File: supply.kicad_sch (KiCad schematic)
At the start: 42 parts

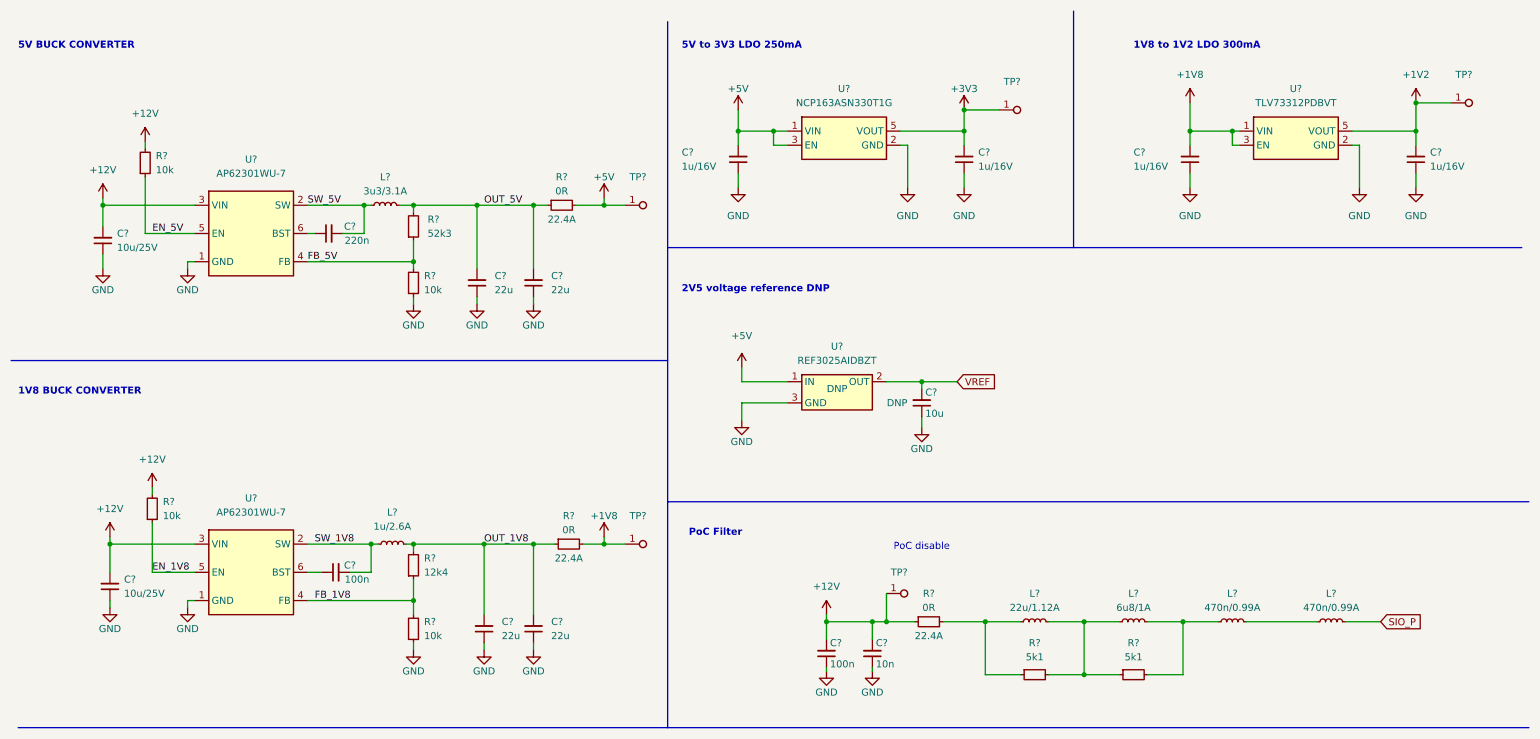
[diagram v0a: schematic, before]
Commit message: Anotate components and fix ERC errors and warnings
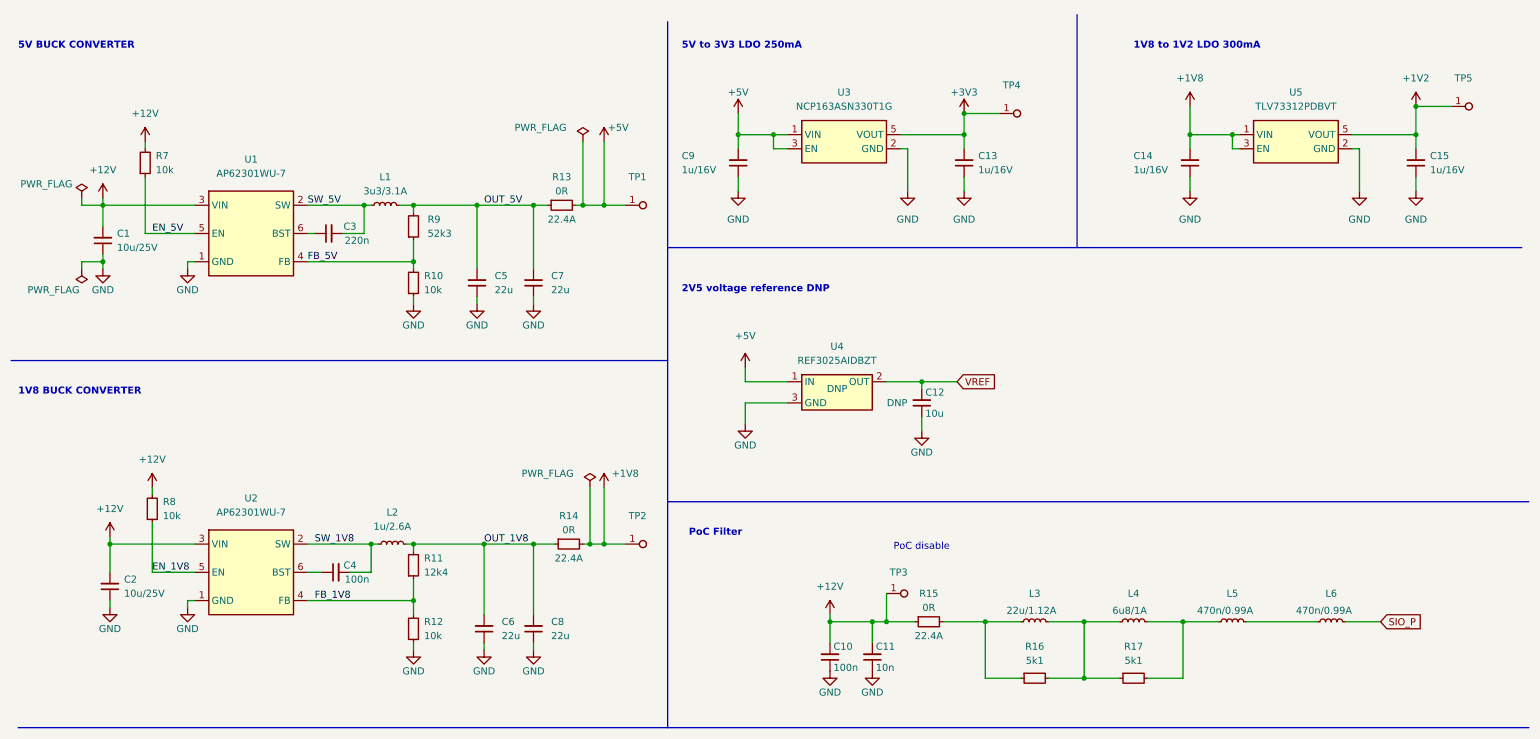
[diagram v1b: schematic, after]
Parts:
- L3: renamed from L?; ISat 0.97A -> 1.12A
- L4: renamed from L?; ISat 1.4 A -> 1 A
- L5, L6: renamed from L?; ISat 0.76 A -> 0.99 A
- gave numbers to parts that had none: 38
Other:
- moved on the sheet: C10, C11, C13, C14, C15, C9, R16, R17, TP4, TP5, U3, U5

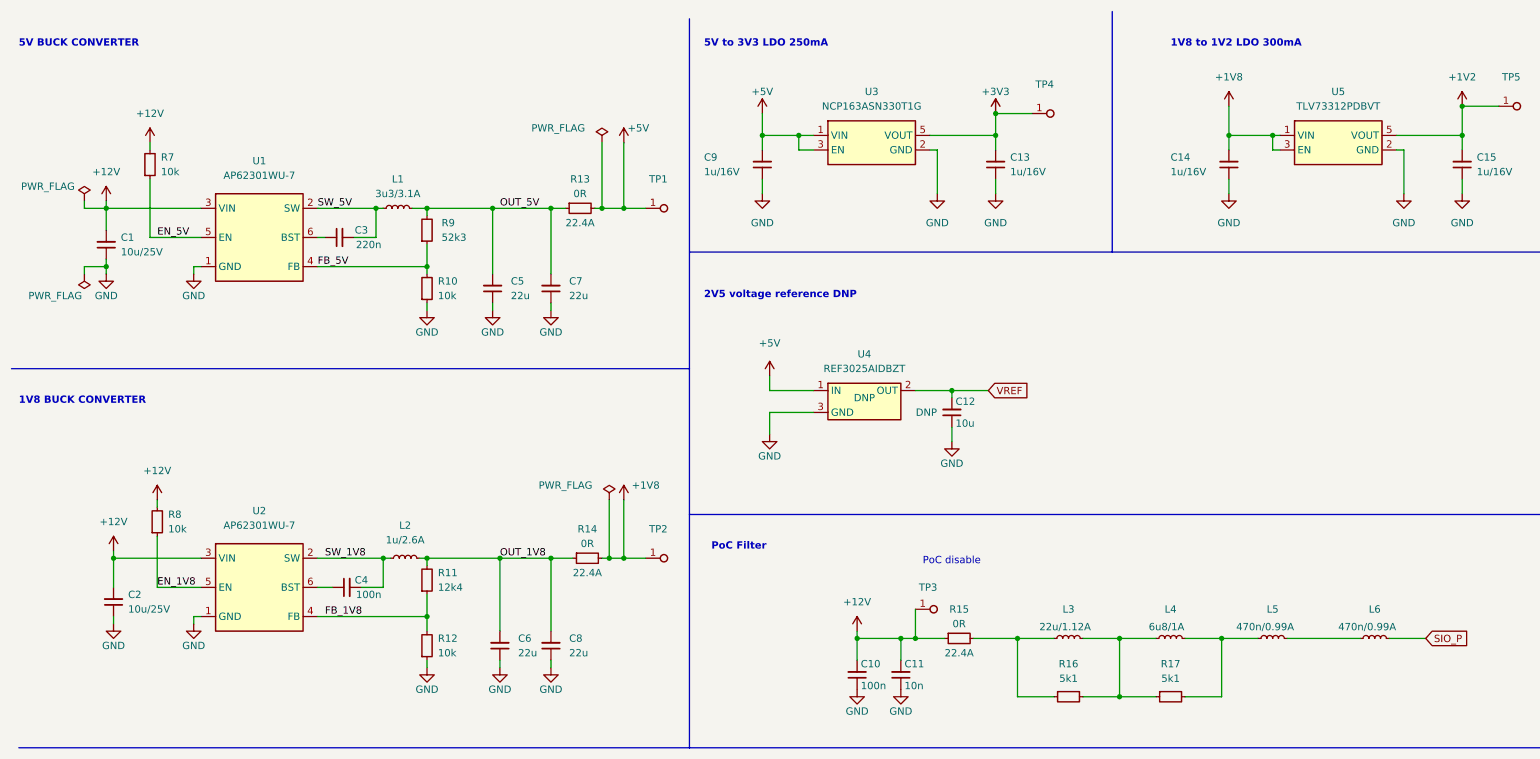
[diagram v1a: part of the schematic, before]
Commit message: Implement changes suggested in design review to schematics
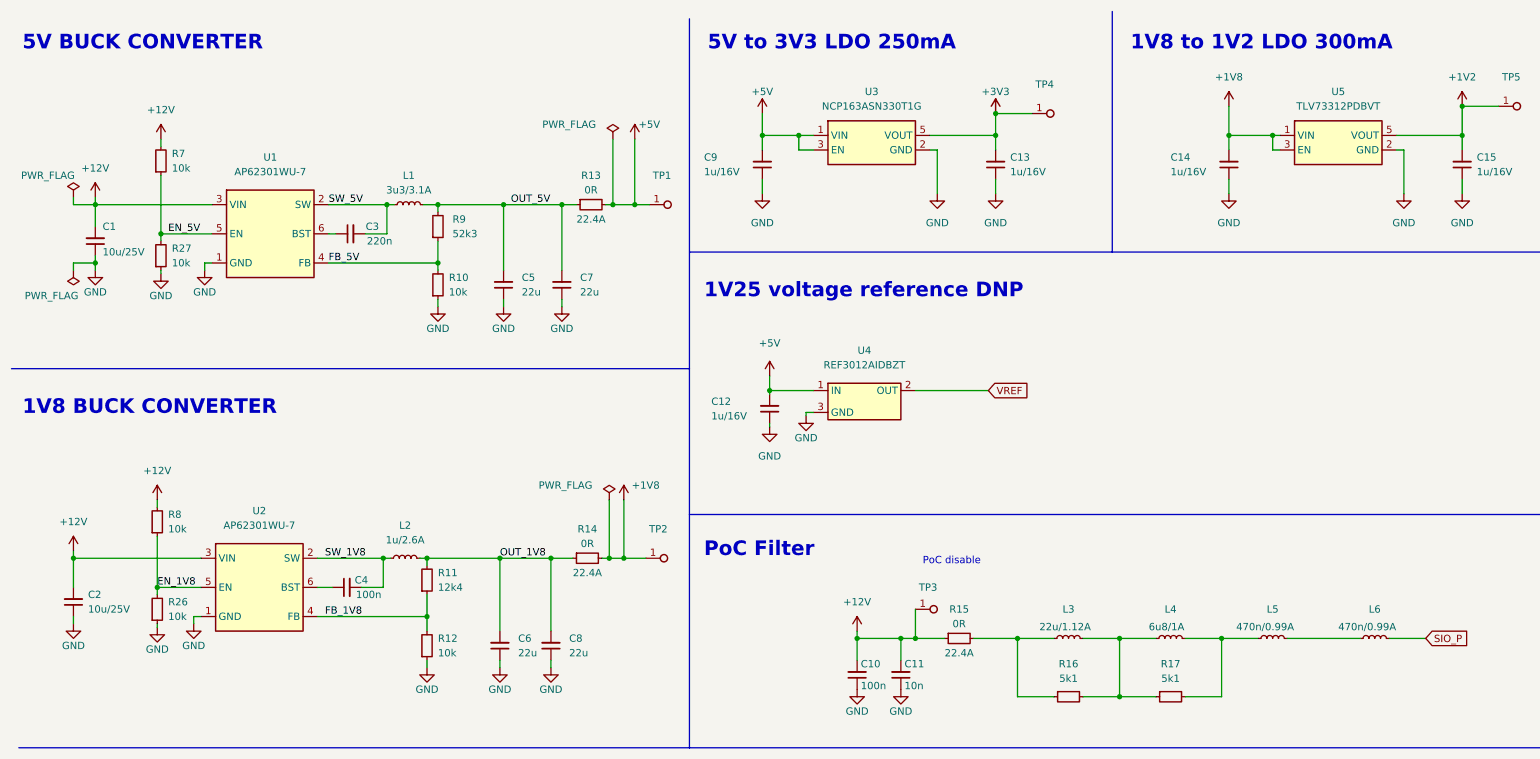
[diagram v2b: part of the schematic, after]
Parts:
- removed C12: C_10u_0402, antmicro-footprints:C_0402_1005Metric, symbol antmicroCapacitors0402:C_10u_0402
- removed U4: REF3025AIDBZT, antmicro-footprints:SOT-23-3, symbol antmicroPMICPowerDistributionSwitchesLoadDrivers:REF3025AIDBZT
- added C12: C_1u_16V_0402, antmicro-footprints:C_0402_1005Metric, symbol antmicroCapacitors0402:C_1u_16V_0402
- added R26, R27: R_10k_0402, antmicro-footprints:R_0402_1005Metric, symbol antmicroResistors0402:R_10k_0402
- added U4: REF3012AIDBZT, antmicro-footprints:SOT-23-3, symbol antmicroPMICPowerDistributionSwitchesLoadDrivers:REF3012AIDBZT
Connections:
- net +5V: now also C12.2, U4.1 (IN)
- net EN_1V8: now also R26.2
- net EN_5V: now also R27.2
- net GND: now also C12.1, R26.1, R27.1, U4.3 (GND)
- net VREF: now also U4.2 (OUT)
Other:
- note added: "1V25 voltage reference DNP"
- note removed: "2V5 voltage reference DNP"
- moved on the sheet: C1, C2, C3, C5, C7, L1, R10, R13, R7, R9, TP1, U1

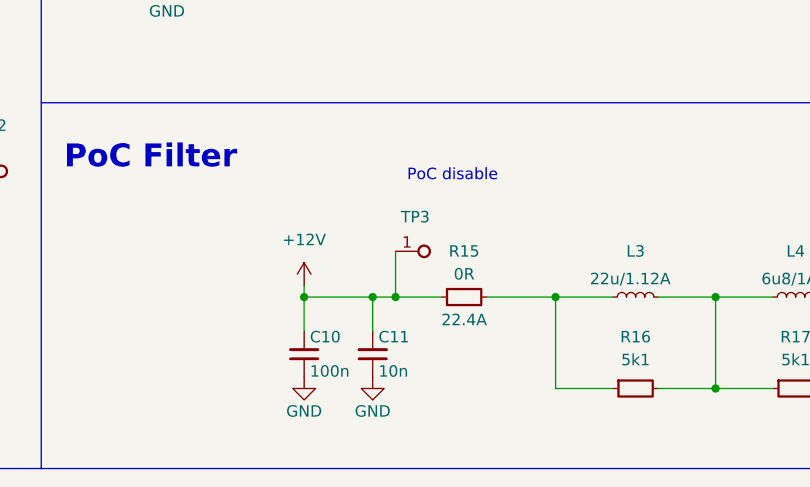
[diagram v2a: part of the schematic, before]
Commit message: Remove R15 and anotate schematic
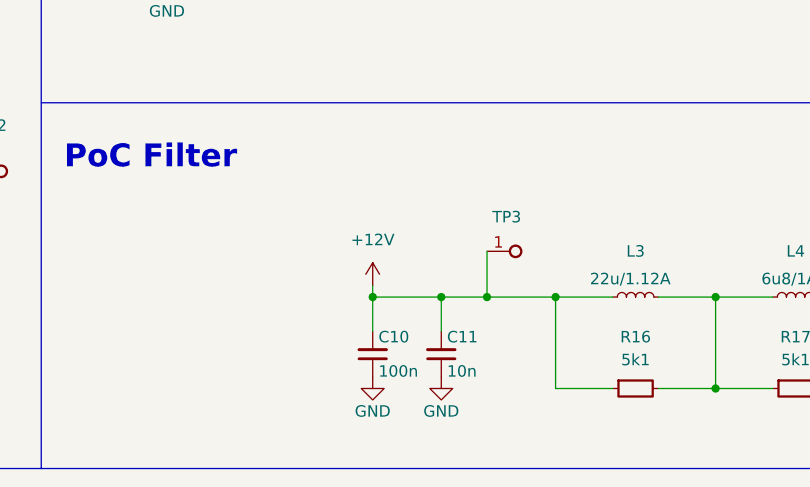
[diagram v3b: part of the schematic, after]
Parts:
- removed R15: R_0R_22.4A_0603, antmicro-footprints:R_0603_1608Metric, symbol antmicroResistors0603:R_0R_22.4A_0603
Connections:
- net +12V: now also L3.1, R16.1
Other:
- note removed: "PoC disable"
- moved on the sheet: C10, C11, TP3

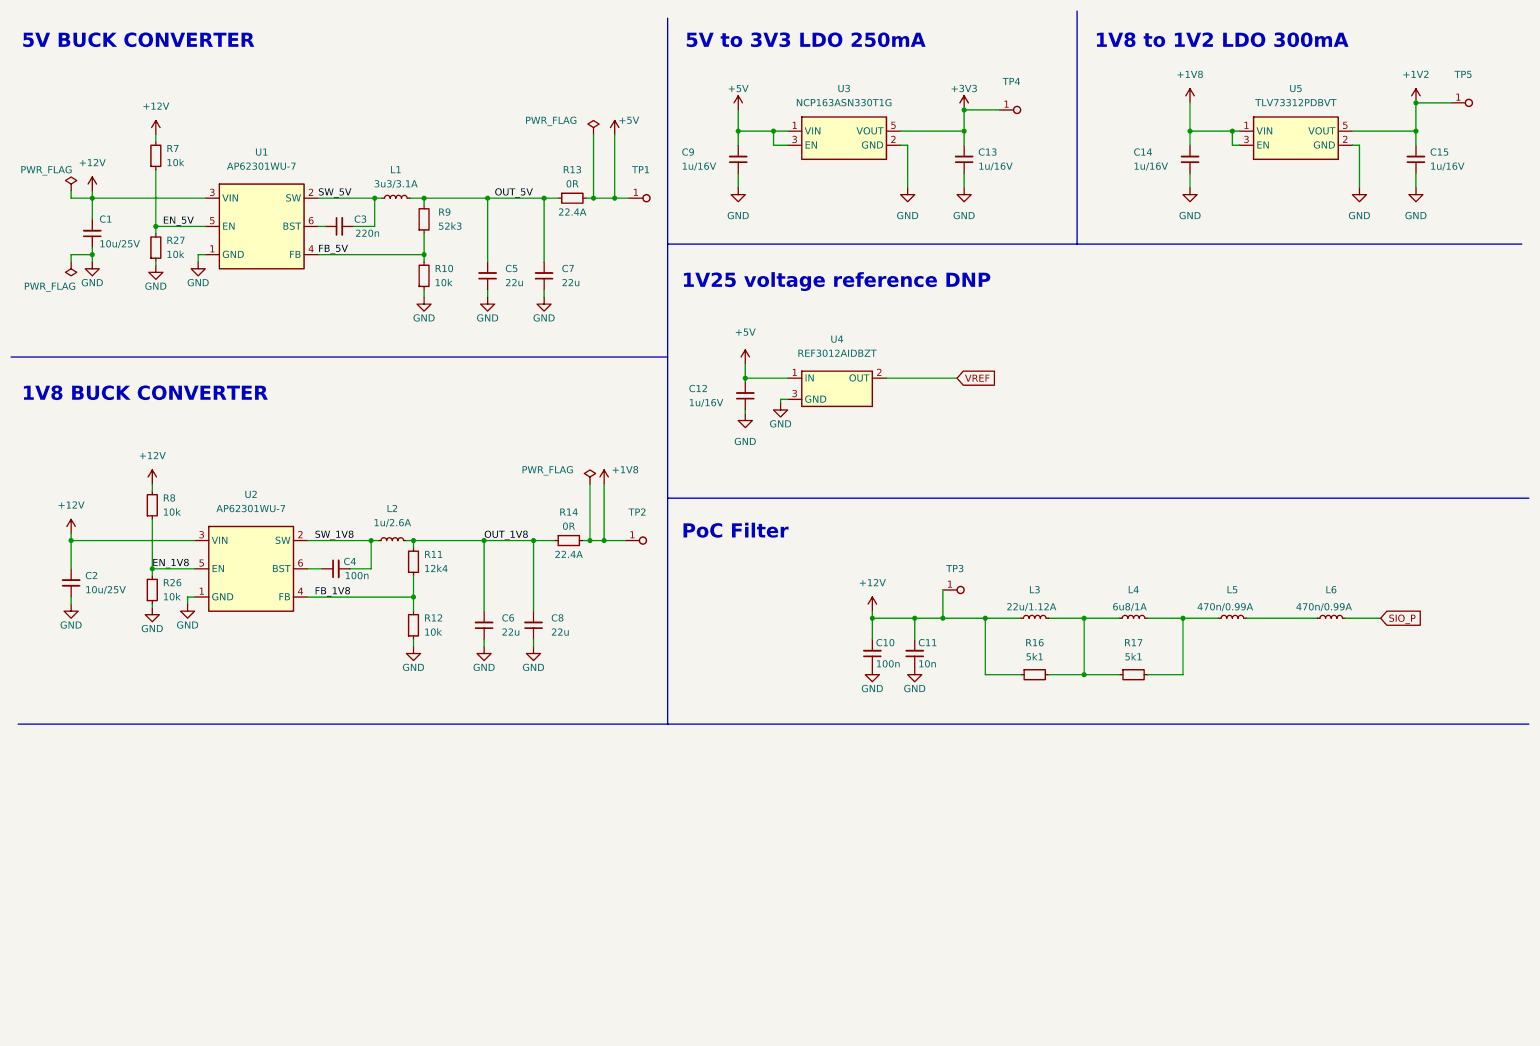
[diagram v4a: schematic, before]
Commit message: [#53377] Rearange supply schematic
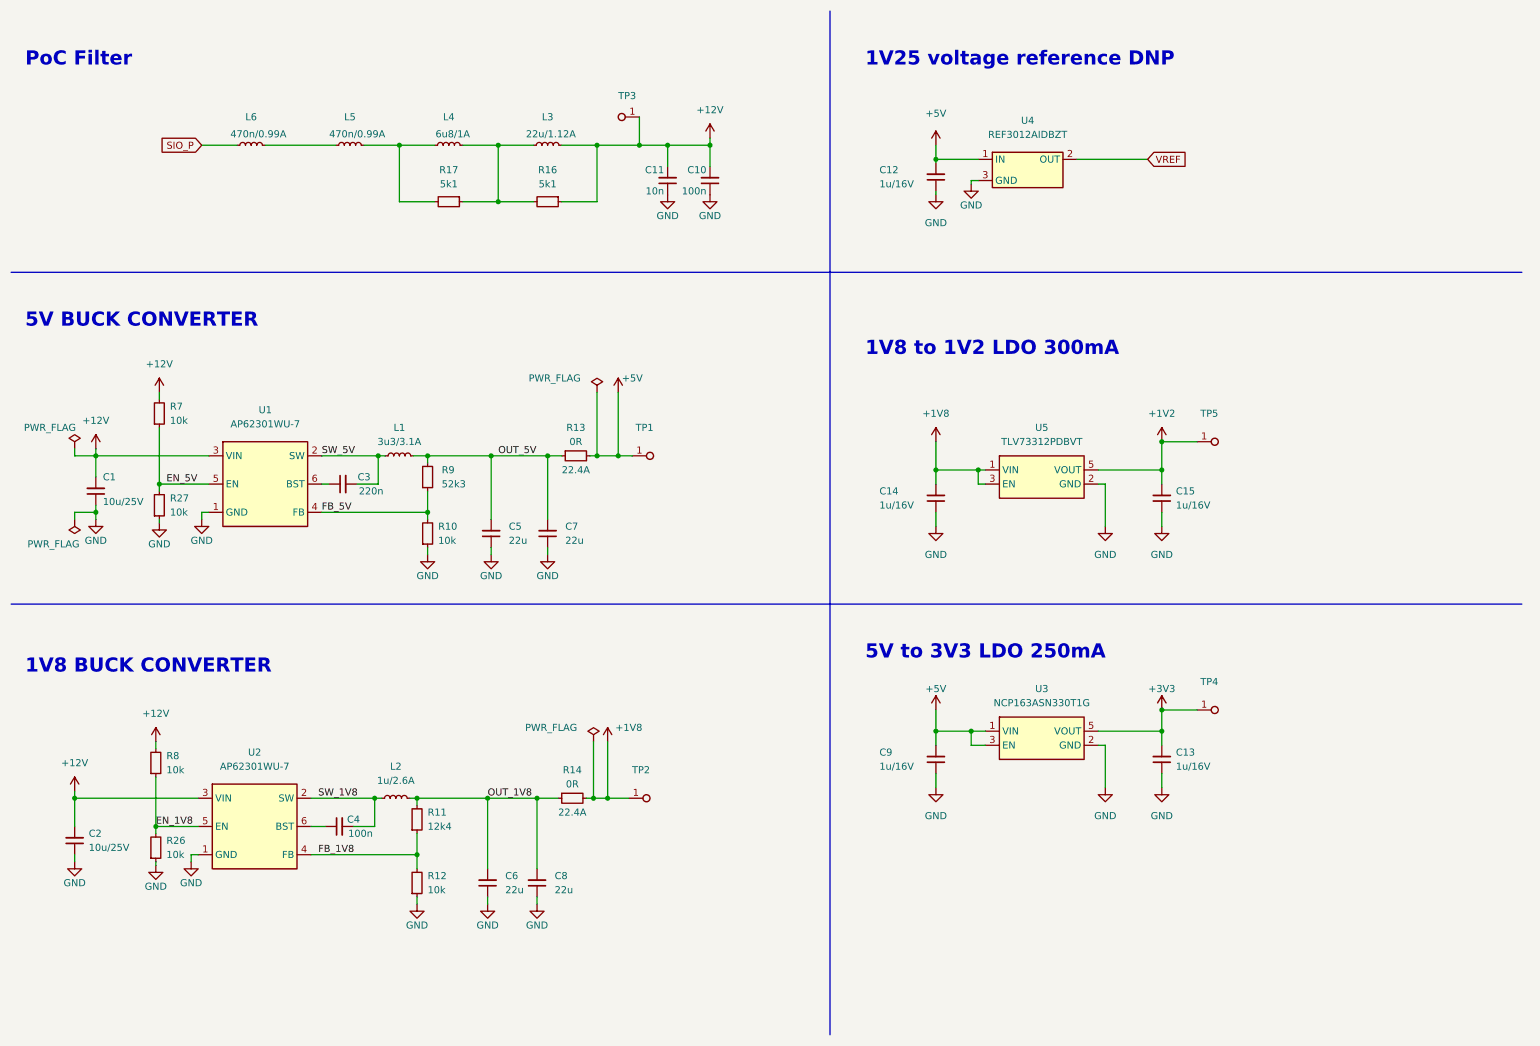
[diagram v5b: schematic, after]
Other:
- moved on the sheet: C1, C10, C11, C12, C13, C14, C15, C2, C3, C4, C5, C6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
